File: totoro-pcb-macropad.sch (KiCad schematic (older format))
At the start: 17 parts, among them J1 USB4085-GF-A_REVA, SW1 SW_PUSH, U1 ATMEGA32U4, X1 XTAL_GND

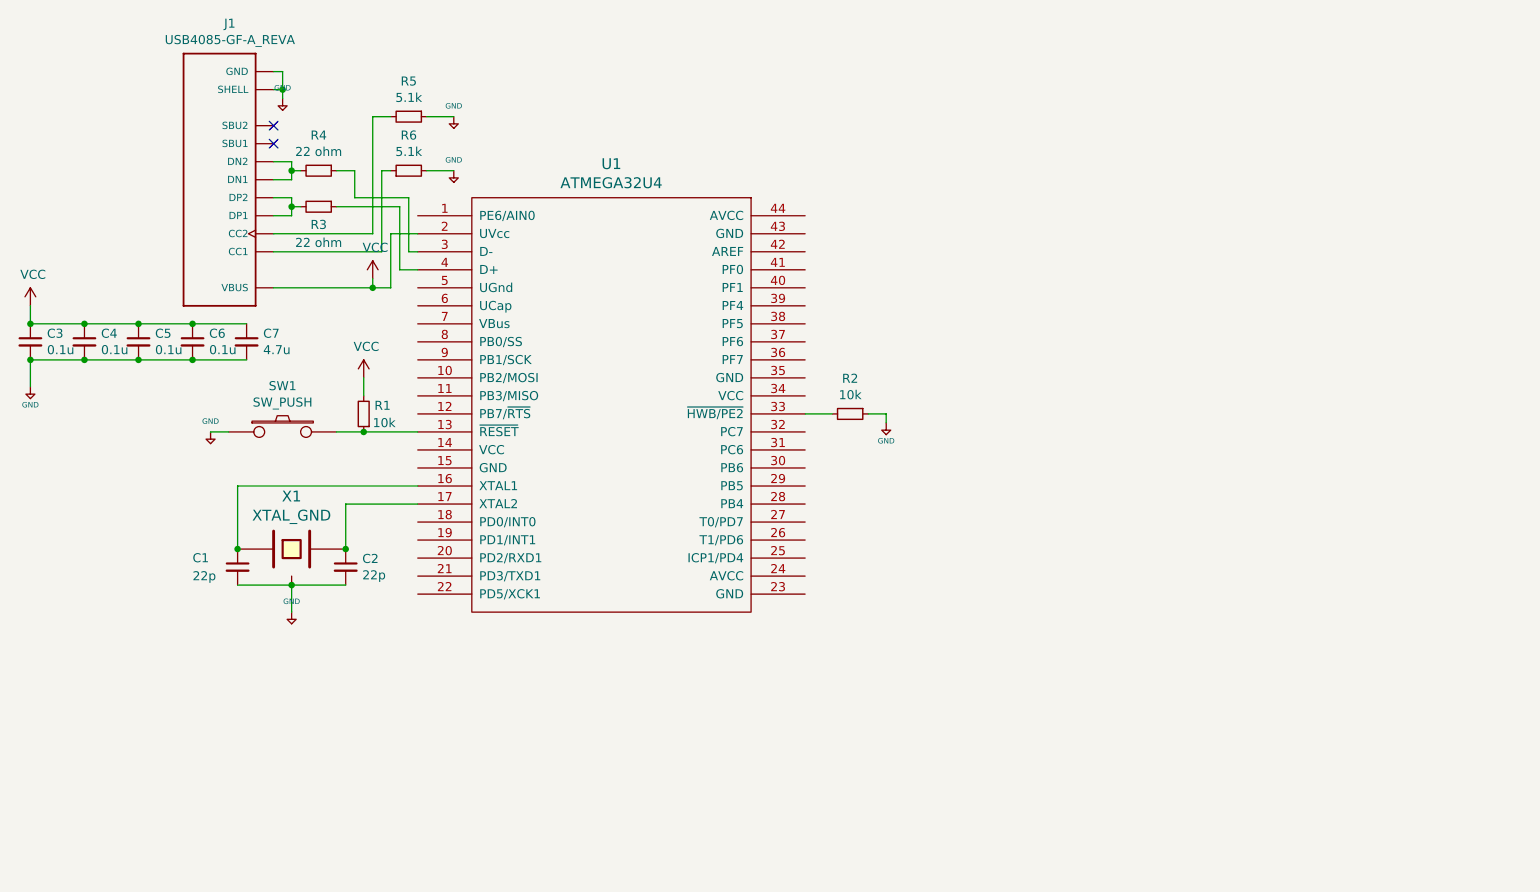
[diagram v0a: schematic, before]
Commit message: Import footprints
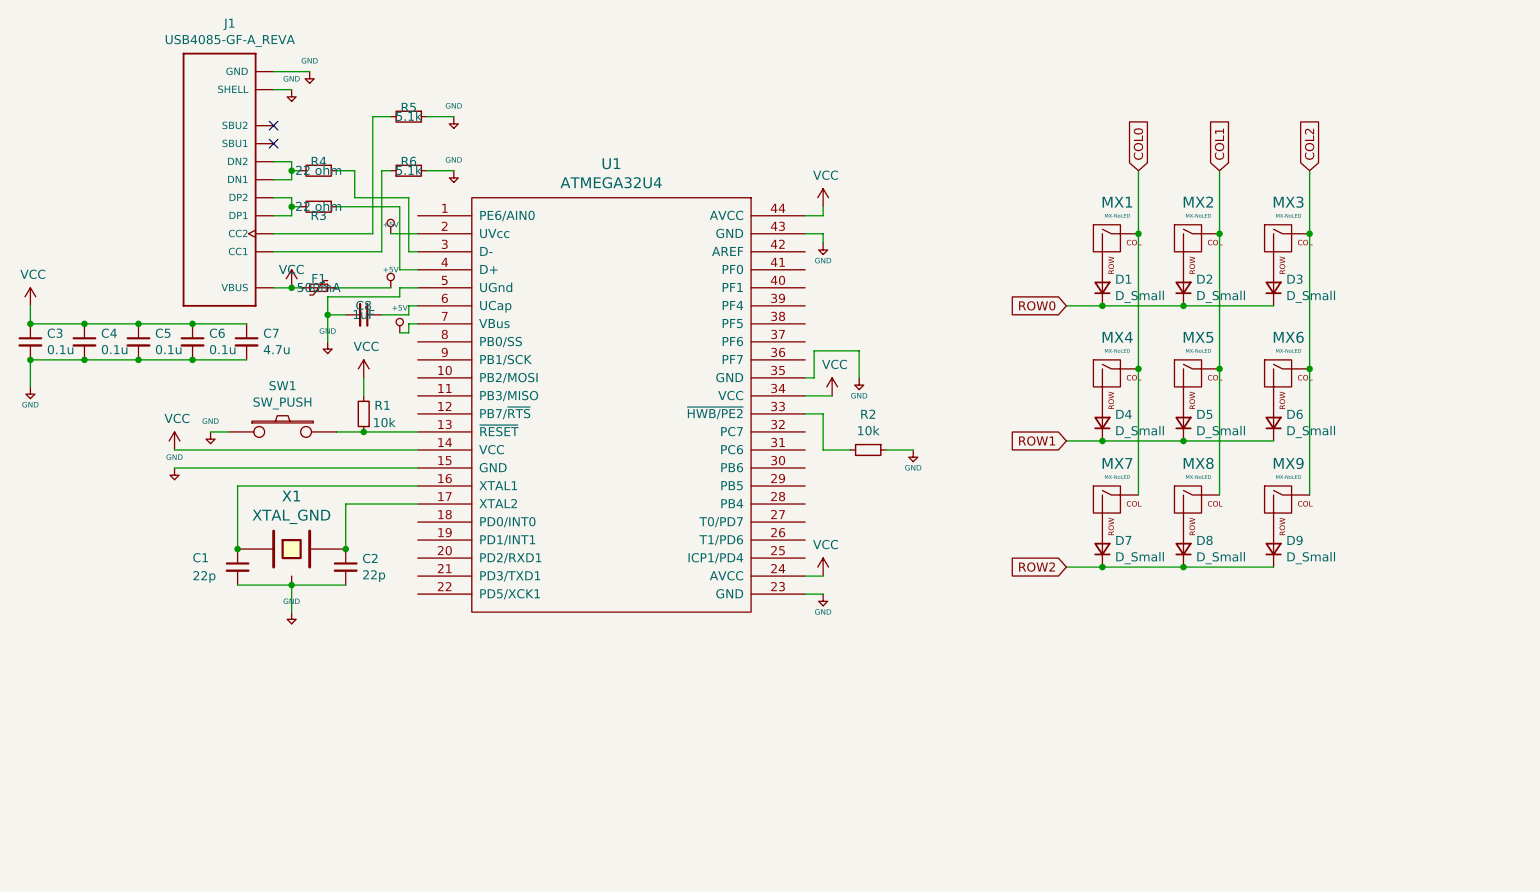
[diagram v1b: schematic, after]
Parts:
- added C8: 1uF, Capacitor_SMD:C_0805_2012Metric_Pad1.15x1.40mm_HandSolder, symbol Device:C_Small
- added D1, D2, D3, D4, D5, D6, D7, D8, D9: D_Small, random-keyboard-parts:D_SOD-123-Pretty, symbol Device:D_Small
- added F1: 500mA, Fuse:Fuse_1206_3216Metric_Pad1.42x1.75mm_HandSolder, symbol Device:Polyfuse_Small
- added MX1, MX2, MX3, MX4, MX5, MX6, MX7, MX8, MX9: MX-NoLED, MX_Only:MXOnly-1U-NoLED, symbol MX_Alps_Hybrid:MX-NoLED
- C1, C2, C3, C4, C5, C6, C7: footprint (none) -> Capacitor_SMD:C_0805_2012Metric_Pad1.15x1.40mm_HandSolder
- J1: footprint GCT_USB4085-GF-A_REVA -> USB4085-GF-A_REVA:GCT_USB4085-GF-A_REVA
- R1, R2, R3, R4, R5, R6: footprint (none) -> Resistor_SMD:R_0805_2012Metric_Pad1.15x1.40mm_HandSolder
- SW1: footprint (none) -> Button_Switch_SMD:SW_SPST_TL3342
- U1: footprint (none) -> Package_QFP:TQFP-44_10x10mm_P0.8mm
- X1: footprint (none) -> Crystal:Crystal_SMD_SeikoEpson_FA238-4Pin_3.2x2.5mm_HandSoldering
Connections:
- net +5V: now also U1.15 (GND), U1.2 (UVcc), U1.23 (GND), U1.35 (GND), U1.43 (GND), U1.5 (UGnd), U1.7 (VBus), C8.2, F1.1
- net VCC: now also U1.14 (VCC), U1.24 (AVCC), U1.34 (VCC), U1.44 (AVCC), F1.2; no longer U1.2 (UVcc)
- net at U1.6 (UCap): now also C8.1
- new net: D1.2 (A), MX1.2 (ROW)
- new net: D2.2 (A), MX2.2 (ROW)
- new net: D3.2 (A), MX3.2 (ROW)
- new net: D6.2 (A), MX6.2 (ROW)
- new net: D5.2 (A), MX5.2 (ROW)
- new net: D4.2 (A), MX4.2 (ROW)
- new net: D7.2 (A), MX7.2 (ROW)
- new net: D8.2 (A), MX8.2 (ROW)
- new net: D9.2 (A), MX9.2 (ROW)
- new net COL0: MX1.1 (COL), MX4.1 (COL), MX7.1 (COL)
- new net COL1: MX2.1 (COL), MX5.1 (COL), MX8.1 (COL)
- new net COL2: MX3.1 (COL), MX6.1 (COL), MX9.1 (COL)
- new net ROW0: D1.1 (K), D2.1 (K), D3.1 (K)
- new net ROW1: D4.1 (K), D5.1 (K), D6.1 (K)
- new net ROW2: D7.1 (K), D8.1 (K), D9.1 (K)
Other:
- moved on the sheet: R2

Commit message: PCB layout
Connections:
- net +5V: now also C3.1, C4.1, C5.1, C6.1, C7.1, R1.2, U1.14 (VCC), U1.24 (AVCC), U1.34 (VCC), U1.44 (AVCC); no longer C1.2, C2.2, C3.2, C4.2, C5.2, C6.2, C7.2, C8.2, J1.A1 (GND), J1.A12 (GND), J1.B1 (GND), J1.B12 (GND), J1.P1 (SHELL), J1.P2 (SHELL), J1.P3 (SHELL), J1.P4 (SHELL), R2.1, R5.1, R6.2, SW1.1, U1.15 (GND), U1.23 (GND), U1.35 (GND), U1.43 (GND), U1.5 (UGnd), X1.3
- net VCC: no longer C3.1, C4.1, C5.1, C6.1, C7.1, R1.2, U1.14 (VCC), U1.24 (AVCC), U1.34 (VCC), U1.44 (AVCC)
- new net GND: C1.2, C2.2, C3.2, C4.2, C5.2, C6.2, C7.2, C8.2, J1.A1 (GND), J1.A12 (GND), J1.B1 (GND), J1.B12 (GND), J1.P1 (SHELL), J1.P2 (SHELL), J1.P3 (SHELL), J1.P4 (SHELL), R2.1, R5.1, R6.2, SW1.1, U1.15 (GND), U1.23 (GND), U1.35 (GND), U1.43 (GND), U1.5 (UGnd), X1.3

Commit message: Final commit
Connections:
- net COL0: now also U1.39 (PF4)
- net COL1: now also U1.40 (PF1)
- net COL2: now also U1.41 (PF0)
- net ROW0: now also U1.38 (PF5)
- net ROW1: now also U1.37 (PF6)
- net ROW2: now also U1.36 (PF7)
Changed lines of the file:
@@
 	2600 2250 2600 2400
-Wire Wire Line
-	5250 1800 5350 1800
-Wire Wire Line
-	5350 1800 5350 1850
 Wire Wire Line
 	5250 1700 5350 1700
@@
 L power:GND #PWR0105
 U 1 1 5F4F7593
-P 5350 1850
-F 0 "#PWR0105" H 5350 1600 50  0001 C CNN
-F 1 "GND" H 5355 1677 50  0000 C CNN
-F 2 "" H 5350 1850 50  0001 C CNN
-F 3 "" H 5350 1850 50  0001 C CNN
-	1    5350 1850
+P 5600 1850
+F 0 "#PWR0105" H 5600 1600 50  0001 C CNN
+F 1 "GND" H 5605 1677 50  0000 C CNN
+F 2 "" H 5600 1850 50  0001 C CNN
+F 3 "" H 5600 1850 50  0001 C CNN
+	1    5600 1850
 	1    0    0    -1
 $EndComp
@@
 	1    0    0    -1
 $EndComp
+Text GLabel 5250 2000 2    50   Input ~ 0
+COL2
+Wire Wire Line
+	5600 1800 5600 1850
+Wire Wire Line
+	5250 1800 5600 1800
+Text GLabel 5250 2100 2    50   Input ~ 0
+COL1
+Text GLabel 5250 2200 2    50   Input ~ 0
+COL0
+Text GLabel 5250 2300 2    50   Input ~ 0
+ROW0
+Text GLabel 5250 2400 2    50   Input ~ 0
+ROW1
+Text GLabel 5250 2500 2    50   Input ~ 0
+ROW2
 $EndSCHEMATC

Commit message: Probably fix crystal footprint, but i dont remember
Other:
- moved on the sheet: C1, C2, C3, C4, C5, C6, C7, C8, D1, D2, D3, D4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
